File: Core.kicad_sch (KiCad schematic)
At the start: 1 part, among them J1 Conn_02x20_Odd_Even

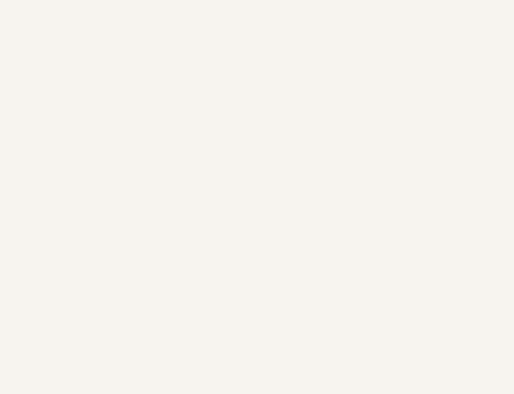
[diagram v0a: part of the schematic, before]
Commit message: DRC Fix for mounting holes
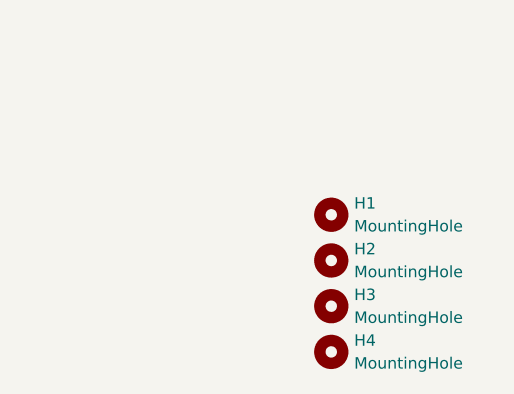
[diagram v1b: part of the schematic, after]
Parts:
- added H1, H2, H3, H4: MountingHole, MountingHole:MountingHole_3.2mm_M3, symbol Mechanical:MountingHole
